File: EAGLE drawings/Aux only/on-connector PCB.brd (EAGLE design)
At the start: 21 x 14 mm, 19 parts, among them IC1 TINY13-20MM0

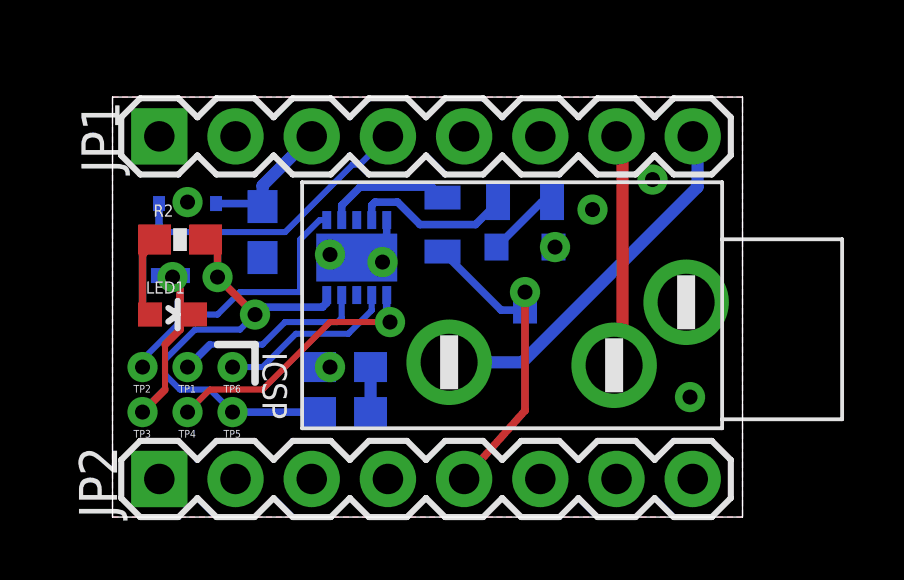
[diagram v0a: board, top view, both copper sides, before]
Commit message: Updated aux-only board, preparing to switch to 32/16/8U2
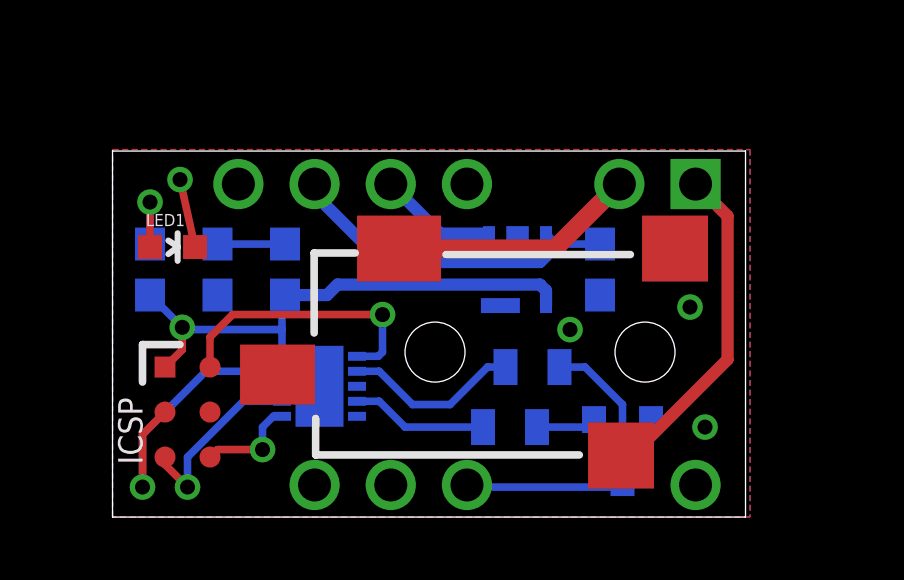
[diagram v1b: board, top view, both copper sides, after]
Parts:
- removed JP1, JP2: (no value), SparkFun:1X08
- added U$1: PANASONIC_CN702_BACKBOARD, personal:040_MLCII_BACK_CN702
- TP1, TP2, TP3, TP4: value TPSQTP06R -> TPSQTP07R; device testpad:TP06R -> testpad:TP07R
- TP5: value TPSQTP06R -> TPSQTP07SQ; device testpad:TP06R -> testpad:TP07SQ
- TP6: value TPSQTP06SQ -> TPSQTP07R; device testpad:TP06SQ -> testpad:TP07R
- U$2: value STEREO_JACK_SJ1-353XNG3NG -> STEREO_JACK_SJ_352X; device personal:3.5MM_SJ1-353XNG -> personal:AUDIO-JACK-3.5MM-SMD
- moved C1 11.3 mm to (16.2, 8.25)
- moved U$7 11.0 mm to (13.5, 8.25)
- moved U$2 7.97 mm to (21.2, 5.50)
- moved R4 7.52 mm to (13.2, 3.00)
- moved U$6 6.60 mm to (17.0, 2.25)
- moved R3 5.62 mm to (14.0, 5.00), turned to 180 degrees
- moved R1 5.35 mm to (3.50, 8.25), turned to 90 degrees
- moved C2 5.15 mm to (5.75, 8.25), turned to 90 degrees
- moved IC1 4.47 mm to (6.90, 4.36), turned to 0 degrees
- moved TP6 3.75 mm to (1.75, 2.00), turned to 90 degrees
- moved TP5 2.70 mm to (1.75, 5.00), turned to 270 degrees
- moved LED1 2.25 mm to (2.00, 9.00)
- moved TP2 2.25 mm to (3.25, 5.00), turned to 90 degrees
- moved TP3 2.25 mm to (3.25, 3.50), turned to 270 degrees
- moved TP1 1.68 mm to (1.75, 3.50), turned to 90 degrees
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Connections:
- net +12: now also U$1.11; no longer JP1.3
- net ACC: now also U$1.9; no longer JP1.4
- net BUS: now also U$1.8; no longer JP2.5
- net GND: now also U$1.10, U$1.2, U$1.7, U$2.SLEEVE; no longer JP1.5, JP2.4, JP2.8, U$2.1
- net ILLUM: now also U$1.13; no longer JP1.2
- net LEFT: now also U$1.3, U$2.TIP; no longer JP1.7, U$2.2
- net MUTE: now also U$1.12; no longer JP2.3
- net RIGHT: now also U$1.1, U$2.RING; no longer JP1.8, U$2.3
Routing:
- net +12: track 4.61 -> 12.0 mm
- net ACC: track 9.78 -> 3.96 mm
- net PB0: track 8.94 -> 3.40 mm, vias 2 -> 1
- net GND: track 7.41 -> 2.30 mm, vias 10 -> 4
- net PB2: track 6.58 -> 10.1 mm
- net PB3: track 4.25 -> 5.93 mm
- net 5V: track 16.5 -> 18.1 mm, vias 3 -> 1
- net RIGHT: track 12.5 -> 11.2 mm
- net PB4: track 5.37 -> 4.56 mm
- net N$1: track 1.50 -> 2.25 mm
- net BUS: track 11.2 -> 10.5 mm, vias 1 -> 0
- net N$2: track 2.77 -> 2.90 mm, vias 0 -> 1
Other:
- board size 21 x 14 mm -> 21.1 x 12.2 mm
